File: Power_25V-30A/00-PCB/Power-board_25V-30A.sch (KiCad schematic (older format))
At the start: 0 parts

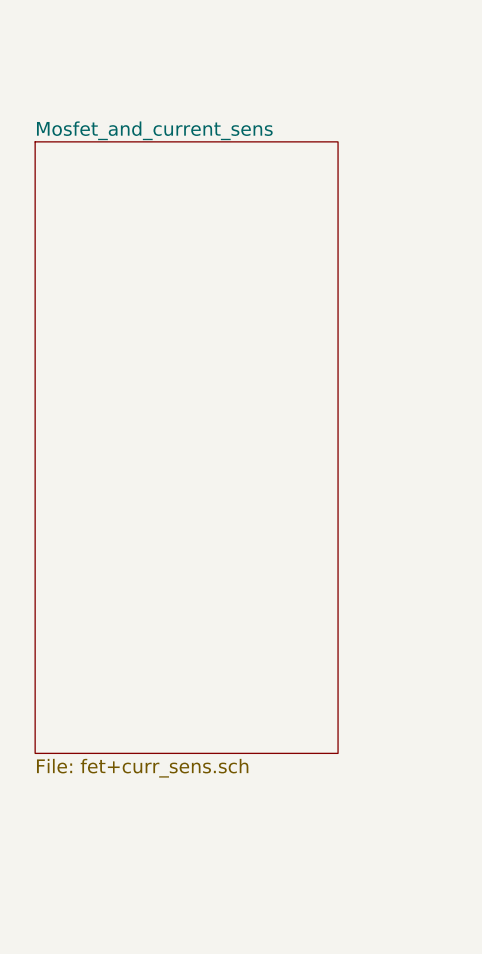
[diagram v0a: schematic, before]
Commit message: Multiplied Phase Schematics
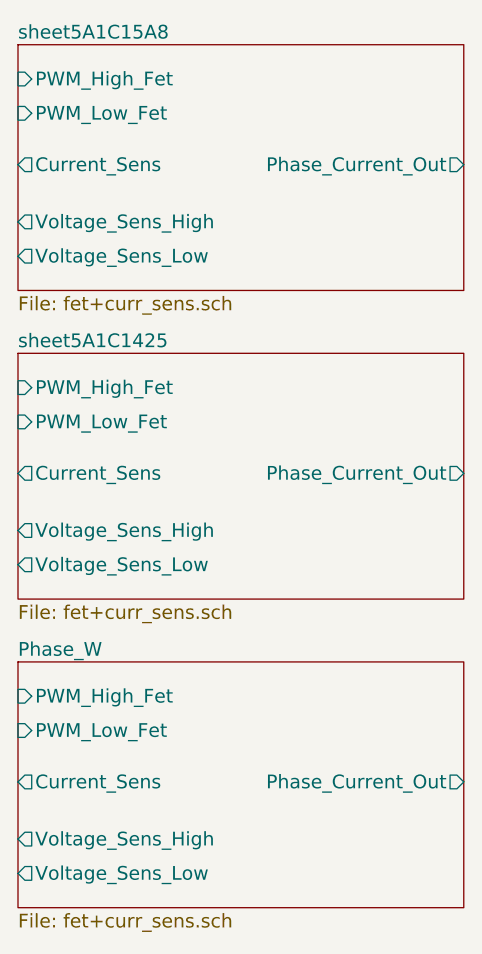
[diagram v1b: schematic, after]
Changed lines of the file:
@@
 EESchema Schematic File Version 4
+LIBS:Power-board_25V-30A-cache
 EELAYER 26 0
 EELAYER END
 $Descr A4 11693 8268
 encoding utf-8
-Sheet 1 2
+Sheet 1 4
 Title ""
 Date ""
@@
 $EndDescr
 $Sheet
-S 5425 1950 1325 2675
-U 5A188E03
-F0 "Mosfet_and_current_sens" 60
+S 5350 4225 1950 1075
+U 5A1BBE2B
+F0 "Phase_W" 60
 F1 "fet+curr_sens.sch" 60
+F2 "PWM_High_Fet" I L 5350 4375 60
+F3 "PWM_Low_Fet" I L 5350 4525 60
+F4 "Current_Sens" O L 5350 4750 60
+F5 "Phase_Current_Out" O R 7300 4750 60
+F6 "Voltage_Sens_Low" O L 5350 5150 60
+F7 "Voltage_Sens_High" O L 5350 5000 60
+$EndSheet
+$Sheet
+S 5350 2875 1950 1075
+U 5A1C142D
+F0 "sheet5A1C1425" 60
+F1 "fet+curr_sens.sch" 60
+F2 "PWM_High_Fet" I L 5350 3025 60
+F3 "PWM_Low_Fet" I L 5350 3175 60
+F4 "Current_Sens" O L 5350 3400 60
+F5 "Phase_Current_Out" O R 7300 3400 60
+F6 "Voltage_Sens_Low" O L 5350 3800 60
+F7 "Voltage_Sens_High" O L 5350 3650 60
+$EndSheet
+$Sheet
+S 5350 1525 1950 1075
+U 5A1C15B0
+F0 "sheet5A1C15A8" 60
+F1 "fet+curr_sens.sch" 60
+F2 "PWM_High_Fet" I L 5350 1675 60
+F3 "PWM_Low_Fet" I L 5350 1825 60
+F4 "Current_Sens" O L 5350 2050 60
+F5 "Phase_Current_Out" O R 7300 2050 60
+F6 "Voltage_Sens_Low" O L 5350 2450 60
+F7 "Voltage_Sens_High" O L 5350 2300 60
 $EndSheet
 $EndSCHEMATC

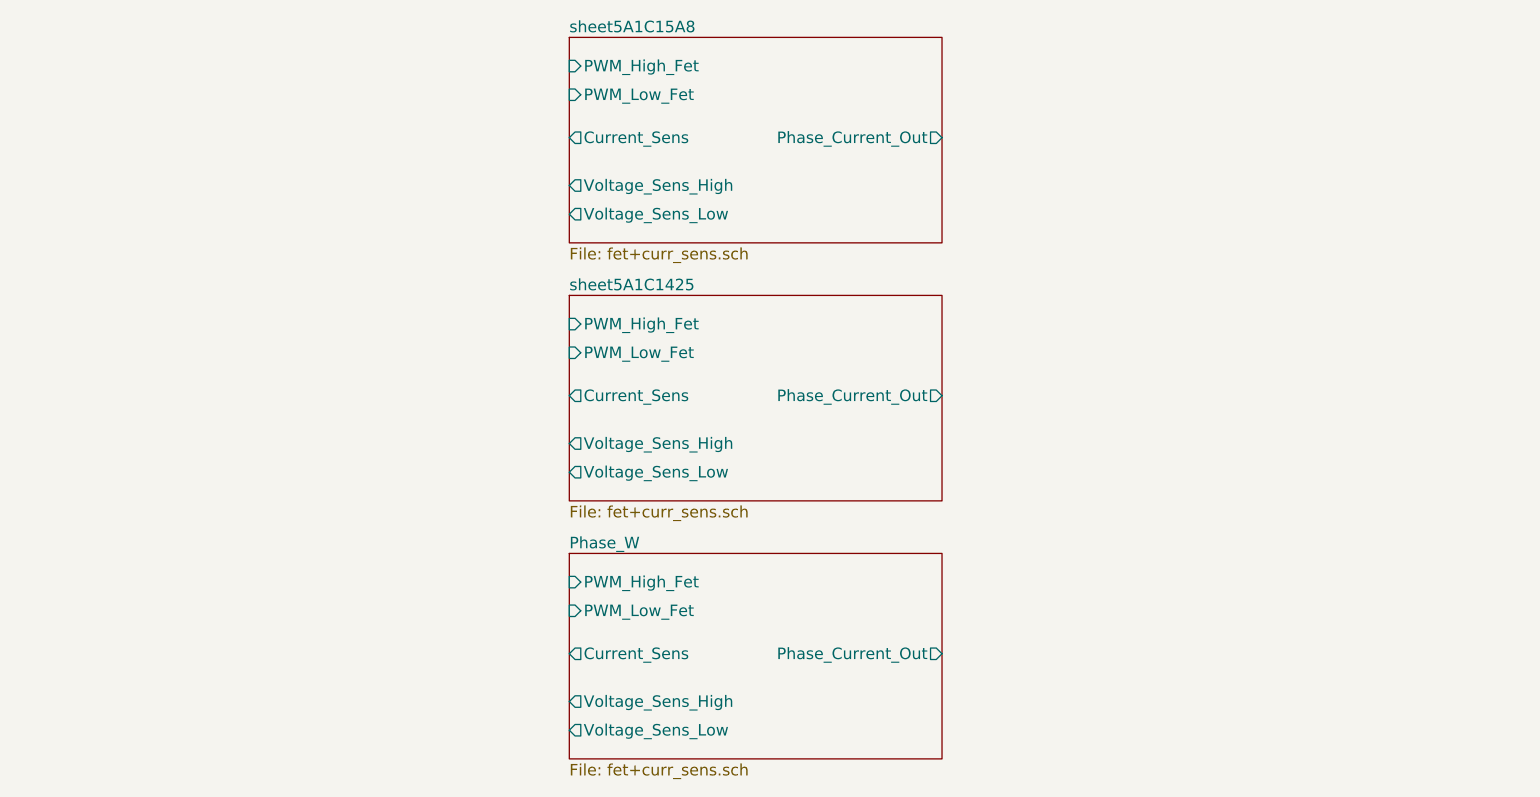
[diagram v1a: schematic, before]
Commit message: testing arrangements for 3 phase power stage
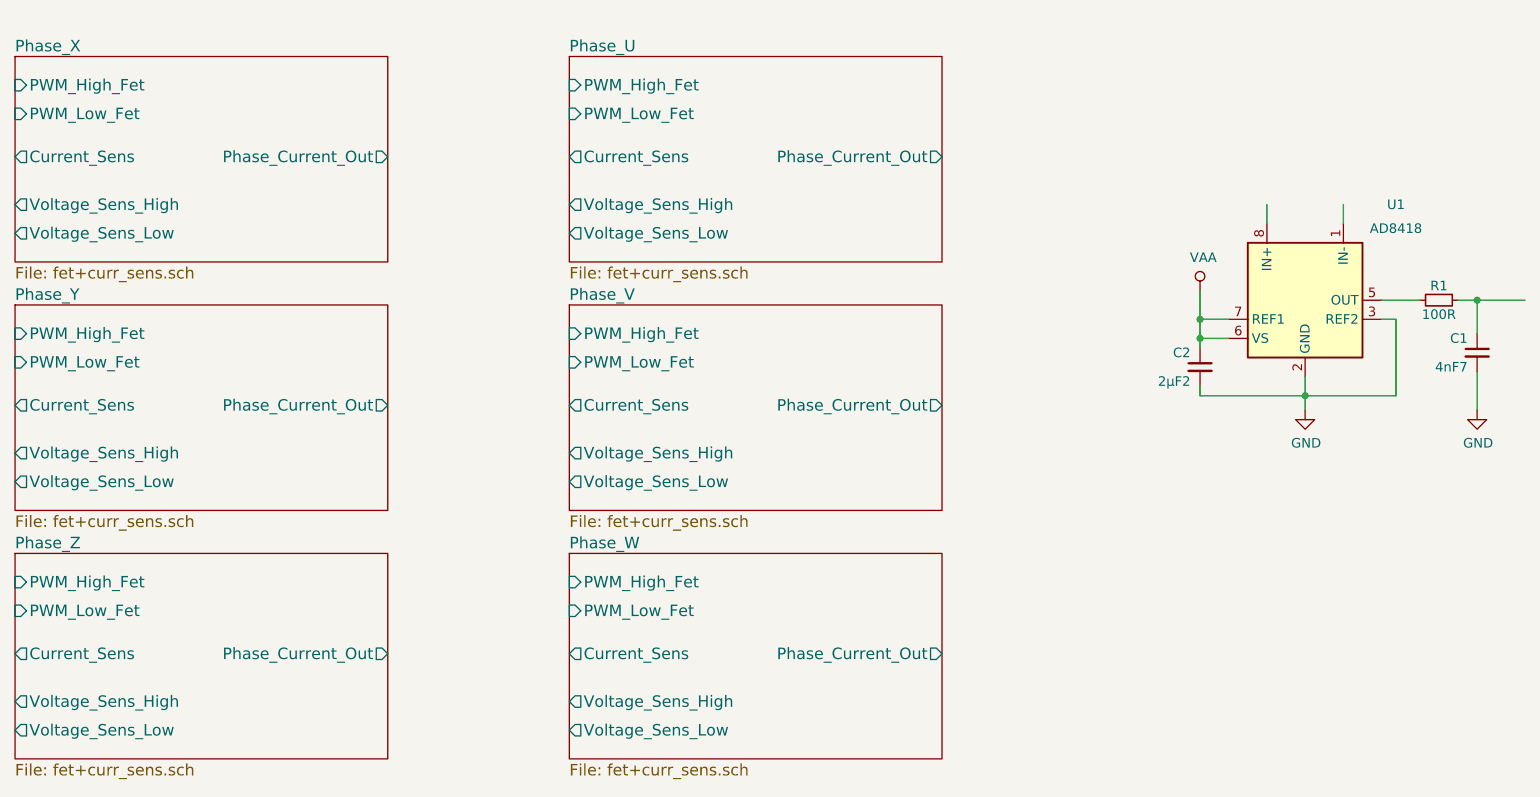
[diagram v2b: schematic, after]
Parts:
- added C1: 4nF7, IPC7351-Nominal:CAPC0603X33, symbol Power-board_25V-30A-rescue:C_Small-RESCUE-Power-board_25V-30A
- added C2: 2µF2, IPC7351-Nominal:CAPC0603X33, symbol Power-board_25V-30A-rescue:C_Small-RESCUE-Power-board_25V-30A
- added R1: 100R, IPC7351-Nominal:RESC0603X30, symbol Power-board_25V-30A-rescue:R_Small-RESCUE-Power-board_25V-30A
- added U1: AD8418, Package_SSOP:MSOP-8_3x3mm_P0.65mm, symbol Power-board_25V-30A-rescue:AD8417-RESCUE-Power-board_25V-30A
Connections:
- net labels added: GND, VAA
- wire segments 0 -> 14
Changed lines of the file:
@@
 $Descr A4 11693 8268
 encoding utf-8
-Sheet 1 4
+Sheet 1 7
 Title ""
 Date ""
@@
 $EndDescr
 $Sheet
+S 5350 1625 1950 1075
+U 5A1BBE2B
+F0 "Phase_U" 60
+F1 "fet+curr_sens.sch" 60
+F2 "PWM_High_Fet" I L 5350 1775 60
+F3 "PWM_Low_Fet" I L 5350 1925 60
+F4 "Current_Sens" O L 5350 2150 60
+F5 "Phase_Current_Out" O R 7300 2150 60
+F6 "Voltage_Sens_Low" O L 5350 2550 60
+F7 "Voltage_Sens_High" O L 5350 2400 60
+$EndSheet
+$Sheet
+S 5350 2925 1950 1075
+U 5A1C142D
+F0 "Phase_V" 60
+F1 "fet+curr_sens.sch" 60
+F2 "PWM_High_Fet" I L 5350 3075 60
+F3 "PWM_Low_Fet" I L 5350 3225 60
+F4 "Current_Sens" O L 5350 3450 60
+F5 "Phase_Current_Out" O R 7300 3450 60
+F6 "Voltage_Sens_Low" O L 5350 3850 60
+F7 "Voltage_Sens_High" O L 5350 3700 60
+$EndSheet
+$Sheet
 S 5350 4225 1950 1075
-U 5A1BBE2B
+U 5A1C15B0
 F0 "Phase_W" 60
 F1 "fet+curr_sens.sch" 60
@@
 F7 "Voltage_Sens_High" O L 5350 5000 60
 $EndSheet
+$Comp
+L Power-board_25V-30A-rescue:AD8417-RESCUE-Power-board_25V-30A U1
+U 1 1 5A226D3C
+P 9200 2900
+F 0 "U1" H 9675 3400 50  0000 C CNN
+F 1 "AD8418" H 9675 3275 50  0000 C CNN
+F 2 "Package_SSOP:MSOP-8_3x3mm_P0.65mm" H 9250 2550 50  0001 C CNN
+F 3 "http://www.analog.com/media/en/technical-documentation/data-sheets/AD8417.pdf" H 9850 2200 50  0001 C CNN
+	1    9200 2900
+	1    0    0    -1
+$EndComp
+Wire Wire Line
+	9000 2500 9000 2400
+Wire Wire Line
+	9400 2400 9400 2500
+Wire Wire Line
+	9200 3300 9200 3475
+$Comp
+L Power-board_25V-30A-rescue:GND-RESCUE-Power-board_25V-30A #PWR02
+U 1 1 5A226D46
+P 9200 3475
+F 0 "#PWR02" H 9200 3225 50  0001 C CNN
+F 1 "GND" H 9205 3302 50  0000 C CNN
+F 2 "" H 9200 3475 50  0001 C CNN
+F 3 "" H 9200 3475 50  0001 C CNN
+	1    9200 3475
+	1    0    0    -1
+$EndComp
+$Comp
+L Power-board_25V-30A-rescue:VAA-RESCUE-Power-board_25V-30A #PWR01
+U 1 1 5A226D4C
+P 8650 2850
+F 0 "#PWR01" H 8650 2700 50  0001 C CNN
+F 1 "VAA" H 8667 3023 50  0000 C CNN
+F 2 "" H 8650 2850 50  0001 C CNN
+F 3 "" H 8650 2850 50  0001 C CNN
+	1    8650 2850
+	1    0    0    -1
+$EndComp
+Wire Wire Line
+	8800 3000 8650 3000
+Wire Wire Line
+	8650 2850 8650 3150
+Wire Wire Line
+	8800 3100 8650 3100
+Connection ~ 8650 3000
+$Comp
+L Power-board_25V-30A-rescue:C_Small-RESCUE-Power-board_25V-30A C2
+U 1 1 5A226D56
+P 8650 3250
+F 0 "C2" H 8700 3325 50  0000 L CNN
+F 1 "2µF2" H 8700 3175 50  0000 L CNN
+F 2 "IPC7351-Nominal:CAPC0603X33" H 8650 3250 50  0001 C CNN
+F 3 "" H 8650 3250 50  0001 C CNN
+	1    8650 3250
+	-1   0    0    -1
+$EndComp
+Connection ~ 8650 3100
+Wire Wire Line
+	8650 3350 8650 3400
+Wire Wire Line
+	8650 3400 9675 3400
+Connection ~ 9200 3400
+Wire Wire Line
+	9600 3000 9675 3000
+Wire Wire Line
+	9675 3000 9675 3400
+Wire Wire Line
+	9600 2900 9800 2900
+$Comp
+L Power-board_25V-30A-rescue:R_Small-RESCUE-Power-board_25V-30A R1
+U 1 1 5A226D64
+P 9900 2900
+F 0 "R1" V 9825 2900 50  0000 C CNN
+F 1 "100R" V 9975 2900 50  0000 C CNN
+F 2 "IPC7351-Nominal:RESC0603X30" H 9900 2900 50  0001 C CNN
+F 3 "" H 9900 2900 50  0001 C CNN
+	1    9900 2900
+	0    1    1    0
+$EndComp
+$Comp
+L Power-board_25V-30A-rescue:C_Small-RESCUE-Power-board_25V-30A C1
+U 1 1 5A226D6B
+P 10100 3175
+F 0 "C1" H 10150 3250 50  0000 L CNN
+F 1 "4nF7" H 10150 3100 50  0000 L CNN
+F 2 "IPC7351-Nominal:CAPC0603X33" H 10100 3175 50  0001 C CNN
+F 3 "" H 10100 3175 50  0001 C CNN
+	1    10100 3175
+	-1   0    0    -1
+$EndComp
+$Comp
+L Power-board_25V-30A-rescue:GND-RESCUE-Power-board_25V-30A #PWR03
+U 1 1 5A226D72
+P 10100 3475
+F 0 "#PWR03" H 10100 3225 50  0001 C CNN
+F 1 "GND" H 10105 3302 50  0000 C CNN
+F 2 "" H 10100 3475 50  0001 C CNN
+F 3 "" H 10100 3475 50  0001 C CNN
+	1    10100 3475
+	1    0    0    -1
+$EndComp
+Wire Wire Line
+	10100 3475 10100 3275
+Wire Wire Line
+	10100 3075 10100 2900
+Wire Wire Line
+	10000 2900 10350 2900
+Connection ~ 10100 2900
 $Sheet
-S 5350 2875 1950 1075
-U 5A1C142D
-F0 "sheet5A1C1425" 60
+S 2450 1625 1950 1075
+U 5A243207
+F0 "Phase_X" 60
 F1 "fet+curr_sens.sch" 60
-F2 "PWM_High_Fet" I L 5350 3025 60
-F3 "PWM_Low_Fet" I L 5350 3175 60
-F4 "Current_Sens" O L 5350 3400 60
-F5 "Phase_Current_Out" O R 7300 3400 60
-F6 "Voltage_Sens_Low" O L 5350 3800 60
-F7 "Voltage_Sens_High" O L 5350 3650 60
+F2 "PWM_High_Fet" I L 2450 1775 60
+F3 "PWM_Low_Fet" I L 2450 1925 60
+F4 "Current_Sens" O L 2450 2150 60
+F5 "Phase_Current_Out" O R 4400 2150 60
+F6 "Voltage_Sens_Low" O L 2450 2550 60
+F7 "Voltage_Sens_High" O L 2450 2400 60
 $EndSheet
 $Sheet
-S 5350 1525 1950 1075
-U 5A1C15B0
-F0 "sheet5A1C15A8" 60
+S 2450 4225 1950 1075
+U 5A256B4E
+F0 "Phase_Z" 60
 F1 "fet+curr_sens.sch" 60
-F2 "PWM_High_Fet" I L 5350 1675 60
-F3 "PWM_Low_Fet" I L 5350 1825 60
-F4 "Current_Sens" O L 5350 2050 60
-F5 "Phase_Current_Out" O R 7300 2050 60
-F6 "Voltage_Sens_Low" O L 5350 2450 60
-F7 "Voltage_Sens_High" O L 5350 2300 60
+F2 "PWM_High_Fet" I L 2450 4375 60
+F3 "PWM_Low_Fet" I L 2450 4525 60
+F4 "Current_Sens" O L 2450 4750 60
+F5 "Phase_Current_Out" O R 4400 4750 60
+F6 "Voltage_Sens_Low" O L 2450 5150 60
+F7 "Voltage_Sens_High" O L 2450 5000 60
+$EndSheet
+$Sheet
+S 2450 2925 1950 1075
+U 5A257414
+F0 "Phase_Y" 60
+F1 "fet+curr_sens.sch" 60
+F2 "PWM_High_Fet" I L 2450 3075 60
+F3 "PWM_Low_Fet" I L 2450 3225 60
+F4 "Current_Sens" O L 2450 3450 60
+F5 "Phase_Current_Out" O R 4400 3450 60
+F6 "Voltage_Sens_Low" O L 2450 3850 60
+F7 "Voltage_Sens_High" O L 2450 3700 60
 $EndSheet
 $EndSCHEMATC
